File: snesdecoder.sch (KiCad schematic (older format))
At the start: 17 parts, among them J1 SNES Controller Input, J2 UpDownLeftRight, J3 AB, J4 XY, J5 StartSel, J6 LR, J7 Power, U1 74HC04, U2 74LS161, U3 TPIC6C596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

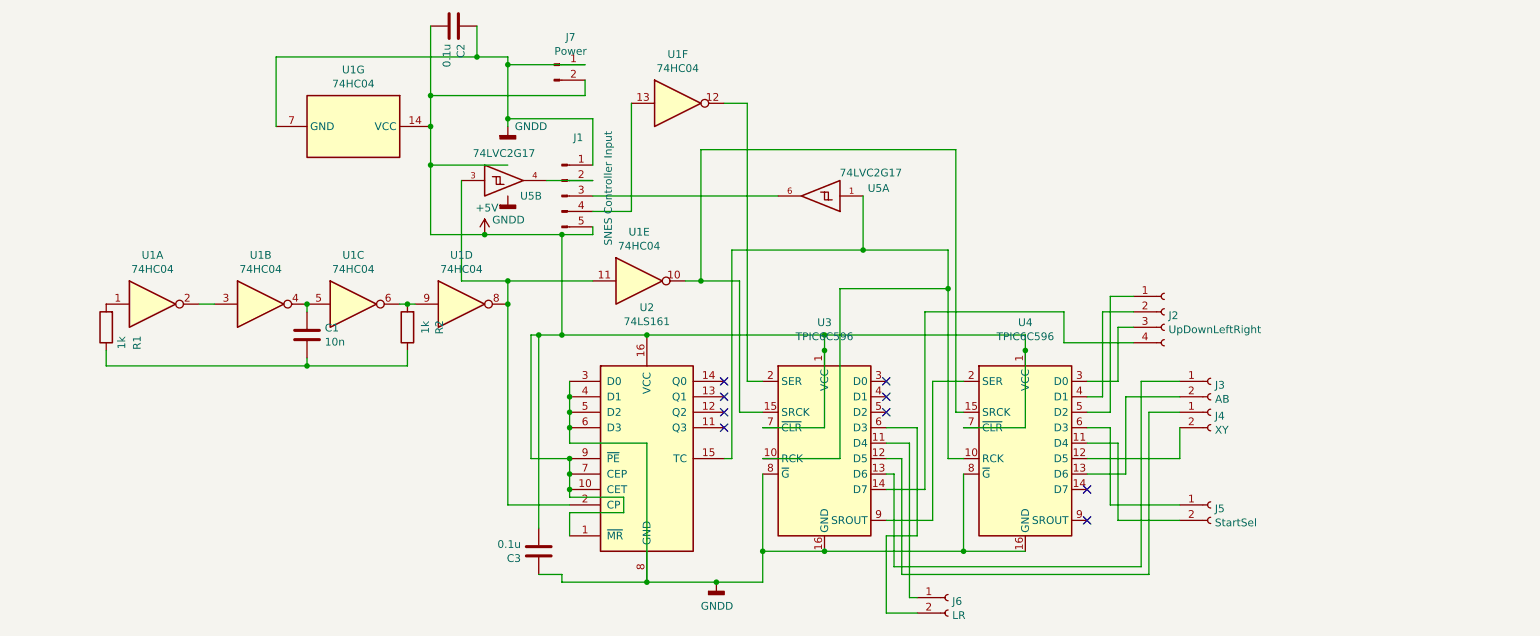
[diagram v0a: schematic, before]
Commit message: update to V2: change schema, pcb layout, datasheets
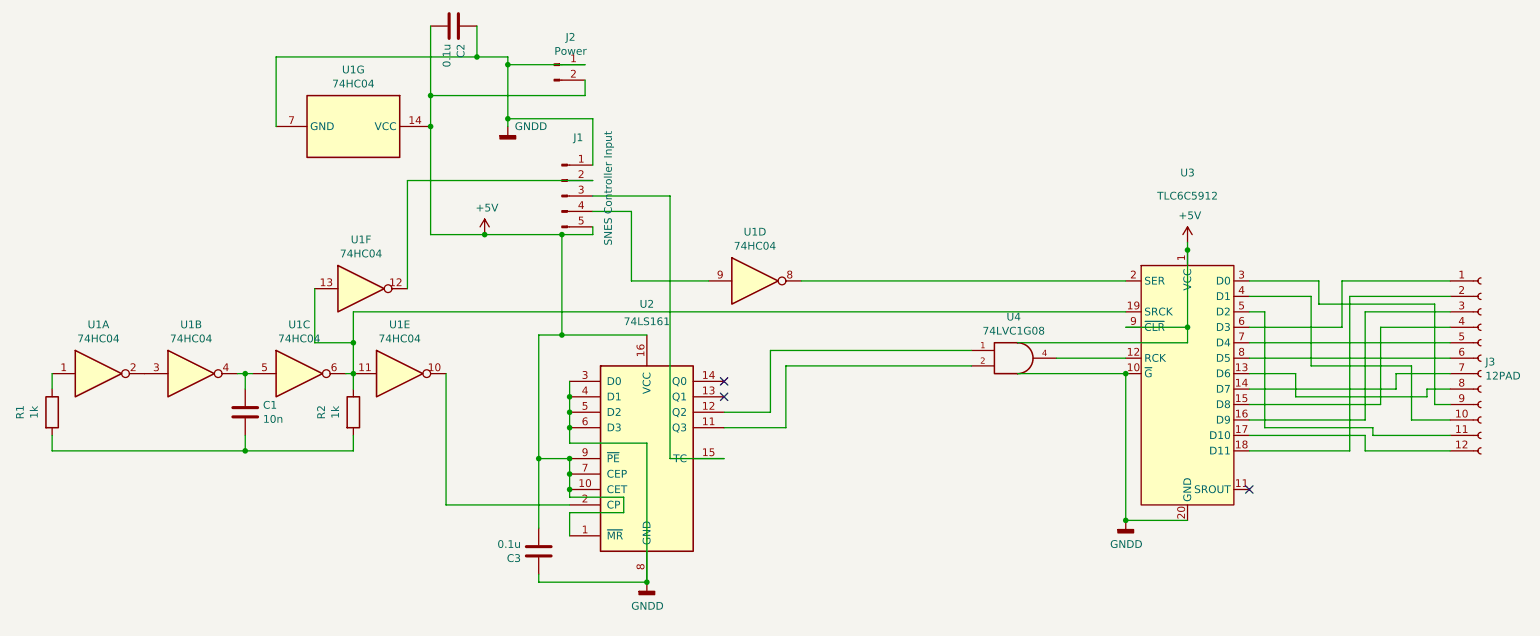
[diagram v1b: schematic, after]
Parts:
- removed J2: UpDownLeftRight, IO:4PAD_DIR, symbol Connector:Conn_01x04_Female
- removed J3: AB, IO:2PAD_AB, symbol Connector:Conn_01x02_Female
- removed J4: XY, IO:2PAD_XY, symbol Connector:Conn_01x02_Female
- removed J5: StartSel, IO:2PAD_StartSel, symbol Connector:Conn_01x02_Female
- removed J6: LR, IO:2PAD_LR, symbol Connector:Conn_01x02_Female
- removed U3, U4: TPIC6C596, Package_SO:SOIC-16_3.9x9.9mm_P1.27mm, symbol newchips:TPIC6C596
- removed U5: 74LVC2G17, Package_SO:SC-74-6_1.5x2.9mm_P0.95mm, symbol 74xGxx:74LVC2G17
- added J3: 12PAD, IO:12PAD, symbol Connector:Conn_01x12_Female
- added U3: TLC6C5912, Package_SO:SOIC-20W_7.5x12.8mm_P1.27mm, symbol newchips:TLC6C5912
- added U4: 74LVC1G08, Package_TO_SOT_SMD:SOT-353_SC-70-5_Handsoldering, symbol 74xGxx:74LVC1G08
- renumbered J7 to J2
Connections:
- net +5V: now also U3.1 (VCC), U3.9 (~CLR), U4.5 (VCC)
- net GND: now also U3.10 (~G), U3.20 (GND), U4.3 (GND)
- net at R1.2: now also C1.2, R2.2; no longer U1.1
- net at U2.11 (Q3): now also U4.2
- net at U2.12 (Q2): now also U4.1
- net at U2.15 (TC): now also J1.3 (Pin_3)
- net at J1.2 (Pin_2): now also U1.12
- net at J1.4 (Pin_4): now also U1.9; no longer U1.13
- net at U1.10: now also U2.2 (CP)
- new net: R2.1, U1.11, U1.13, U1.6, U3.19 (SRCK)
- new net: J3.1 (Pin_1), U3.6 (D3)
- new net: J3.10 (Pin_10), U3.4 (D1)
- new net: J3.11 (Pin_11), U3.5 (D2)
- new net: J3.12 (Pin_12), U3.17 (D10)
- new net: J3.2 (Pin_2), U3.18 (D11)
- new net: J3.3 (Pin_3), U3.16 (D9)
- new net: J3.4 (Pin_4), U3.15 (D8)
- new net: J3.5 (Pin_5), U3.7 (D4)
- new net: J3.6 (Pin_6), U3.8 (D5)
- new net: J3.7 (Pin_7), U3.14 (D7)
- new net: J3.8 (Pin_8), U3.13 (D6)
- new net: J3.9 (Pin_9), U3.3 (D0)
- new net: R1.1, U1.1
- new net: U3.12 (RCK), U4.4
- new net: U1.8, U3.2 (SER)
- no-connect marks 9 -> 3
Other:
- moved on the sheet: C1, R2

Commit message: gerbers to v2
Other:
- moved on the sheet: J3, U3, U4
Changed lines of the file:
@@
 L newchips:TLC6C5912 U3
 U 1 1 5FB36650
-P 8200 3350
-F 0 "U3" H 8200 4450 50  0000 C CNN
-F 1 "TLC6C5912" H 8200 4300 50  0000 C CNN
-F 2 "Package_SO:SOIC-20W_7.5x12.8mm_P1.27mm" H 8600 2650 50  0001 C CNN
-F 3 "" H 8600 2650 50  0001 C CNN
-	1    8200 3350
-	1    0    0    -1
-$EndComp
-Wire Wire Line
-	5700 2950 7800 2950
-Wire Wire Line
-	7350 3450 7800 3450
-Wire Wire Line
-	7800 3550 7800 4500
-Wire Wire Line
-	7800 4500 8200 4500
+P 7000 3350
+F 0 "U3" H 7000 4450 50  0000 C CNN
+F 1 "TLC6C5912" H 7000 4300 50  0000 C CNN
+F 2 "Package_SO:SOIC-20W_7.5x12.8mm_P1.27mm" H 7400 2650 50  0001 C CNN
+F 3 "" H 7400 2650 50  0001 C CNN
+	1    7000 3350
+	1    0    0    -1
+$EndComp
+Wire Wire Line
+	6150 3450 6600 3450
+Wire Wire Line
+	6600 3550 6600 4500
+Wire Wire Line
+	6600 4500 7000 4500
 $Comp
 L power:GNDD #PWR0101
 U 1 1 5FB3EC8C
-P 7800 4500
-F 0 "#PWR0101" H 7800 4250 50  0001 C CNN
-F 1 "GNDD" H 7804 4345 50  0000 C CNN
-F 2 "" H 7800 4500 50  0001 C CNN
-F 3 "" H 7800 4500 50  0001 C CNN
-	1    7800 4500
-	1    0    0    -1
-$EndComp
-Connection ~ 7800 4500
+P 6600 4500
+F 0 "#PWR0101" H 6600 4250 50  0001 C CNN
+F 1 "GNDD" H 6604 4345 50  0000 C CNN
+F 2 "" H 6600 4500 50  0001 C CNN
+F 3 "" H 6600 4500 50  0001 C CNN
+	1    6600 4500
+	1    0    0    -1
+$EndComp
+Connection ~ 6600 4500
 $Comp
 L power:+5V #PWR0102
 U 1 1 5FB41555
-P 8200 2700
-F 0 "#PWR0102" H 8200 2550 50  0001 C CNN
-F 1 "+5V" H 8215 2873 50  0000 C CNN
-F 2 "" H 8200 2700 50  0001 C CNN
-F 3 "" H 8200 2700 50  0001 C CNN
-	1    8200 2700
+P 7000 2700
+F 0 "#PWR0102" H 7000 2550 50  0001 C CNN
+F 1 "+5V" H 7015 2873 50  0000 C CNN
+F 2 "" H 7000 2700 50  0001 C CNN
+F 3 "" H 7000 2700 50  0001 C CNN
+	1    7000 2700
 	1    0    0    -1
 $EndComp
@@
 	4850 2400 4350 2400
 Wire Wire Line
-	7800 3250 8200 3250
-Wire Wire Line
-	8200 3250 8200 2750
-Wire Wire Line
-	8200 2750 8200 2700
-Connection ~ 8200 2750
+	6600 3250 7000 3250
+Wire Wire Line
+	7000 3250 7000 2750
+Wire Wire Line
+	7000 2750 7000 2700
+Connection ~ 7000 2750
 NoConn ~ 5200 3600
 NoConn ~ 5200 3700
-NoConn ~ 8600 4300
+NoConn ~ 7400 4300
 $Comp
 L 74xGxx:74LVC1G08 U4
 U 1 1 5FB0C867
-P 7100 3450
-F 0 "U4" H 7075 3717 50  0000 C CNN
-F 1 "74LVC1G08" H 7075 3626 50  0000 C CNN
-F 2 "Package_TO_SOT_SMD:SOT-353_SC-70-5_Handsoldering" H 7100 3450 50  0001 C CNN
-F 3 "http://www.ti.com/lit/sg/scyt129e/scyt129e.pdf" H 7100 3450 50  0001 C CNN
-	1    7100 3450
+P 5900 3450
+F 0 "U4" H 5875 3717 50  0000 C CNN
+F 1 "74LVC1G08" H 5875 3626 50  0000 C CNN
+F 2 "Package_TO_SOT_SMD:SOT-353_SC-70-5_Handsoldering" H 5900 3450 50  0001 C CNN
+F 3 "http://www.ti.com/lit/sg/scyt129e/scyt129e.pdf" H 5900 3450 50  0001 C CNN
+	1    5900 3450
 	1    0    0    -1
 $EndComp
@@
 	5500 3800 5500 3400
 Wire Wire Line
-	5500 3400 6800 3400
-Wire Wire Line
 	5600 3900 5600 3500
 Wire Wire Line
-	5600 3500 6800 3500
-Wire Wire Line
 	5200 3900 5600 3900
 Wire Wire Line
-	7100 3350 8200 3350
-Wire Wire Line
-	8200 3350 8200 3250
-Connection ~ 8200 3250
-Wire Wire Line
-	7100 3550 7800 3550
-Connection ~ 7800 3550
+	5900 3350 7000 3350
+Wire Wire Line
+	7000 3350 7000 3250
+Connection ~ 7000 3250
+Wire Wire Line
+	5900 3550 6600 3550
+Connection ~ 6600 3550
 $Comp
 L Device:R R2
@@
 Wire Wire Line
 	2800 3150 2800 3350
-Wire Wire Line
-	2800 3150 7800 3150
 Connection ~ 2800 3350
 $Comp
 L Connector:Conn_01x12_Female J3
 U 1 1 5FAF303D
-P 10100 3450
-F 0 "J3" H 10128 3426 50  0000 L CNN
-F 1 "12PAD" H 10128 3335 50  0000 L CNN
-F 2 "IO:12PAD" H 10100 3450 50  0001 C CNN
-F 3 "~" H 10100 3450 50  0001 C CNN
-	1    10100 3450
-	1    0    0    -1
-$EndComp
-Wire Wire Line
-	8600 4050 9250 4050
-Wire Wire Line
-	9250 4050 9250 3050
-Wire Wire Line
-	9250 3050 9900 3050
-Wire Wire Line
-	8600 3950 9350 3950
-Wire Wire Line
-	9350 3950 9350 4050
-Wire Wire Line
-	9350 4050 9900 4050
-Wire Wire Line
-	8600 3850 9350 3850
-Wire Wire Line
-	9350 3850 9350 3150
-Wire Wire Line
-	9350 3150 9900 3150
-Wire Wire Line
-	8600 3750 9450 3750
-Wire Wire Line
-	9450 3750 9450 3250
-Wire Wire Line
-	9450 3250 9900 3250
-Wire Wire Line
-	9550 3650 9550 3550
-Wire Wire Line
-	9550 3550 9900 3550
-Wire Wire Line
-	8600 3650 9550 3650
-Wire Wire Line
-	8600 3550 8900 3550
-Wire Wire Line
-	8900 3550 8900 3700
-Wire Wire Line
-	8900 3700 9750 3700
-Wire Wire Line
-	9750 3700 9750 3650
-Wire Wire Line
-	9750 3650 9900 3650
-Wire Wire Line
-	8600 3450 9900 3450
-Wire Wire Line
-	9900 3350 8600 3350
-Wire Wire Line
-	8600 3250 9200 3250
-Wire Wire Line
-	9200 3250 9200 2950
-Wire Wire Line
-	9200 2950 9900 2950
-Wire Wire Line
-	8600 3150 8700 3150
-Wire Wire Line
-	8700 3150 8700 3900
-Wire Wire Line
-	8700 3900 9400 3900
-Wire Wire Line
-	9400 3900 9400 3950
-Wire Wire Line
-	9400 3950 9900 3950
-Wire Wire Line
-	8600 3050 9000 3050
-Wire Wire Line
-	9000 3050 9000 3500
-Wire Wire Line
-	9000 3500 9650 3500
-Wire Wire Line
-	9650 3500 9650 3850
-Wire Wire Line
-	9650 3850 9900 3850
-Wire Wire Line
-	9900 3750 9800 3750
-Wire Wire Line
-	9800 3750 9800 3100
-Wire Wire Line
-	9800 3100 9050 3100
-Wire Wire Line
-	9050 3100 9050 2950
-Wire Wire Line
-	9050 2950 8600 2950
+P 8900 3450
+F 0 "J3" H 8928 3426 50  0000 L CNN
+F 1 "12PAD" H 8928 3335 50  0000 L CNN
+F 2 "IO:12PAD" H 8900 3450 50  0001 C CNN
+F 3 "~" H 8900 3450 50  0001 C CNN
+	1    8900 3450
+	1    0    0    -1
+$EndComp
+Wire Wire Line
+	7400 4050 8050 4050
+Wire Wire Line
+	8050 4050 8050 3050
+Wire Wire Line
+	8050 3050 8700 3050
+Wire Wire Line
+	7400 3950 8150 3950
+Wire Wire Line
+	8150 3950 8150 4050
+Wire Wire Line
+	8150 4050 8700 4050
+Wire Wire Line
+	7400 3850 8150 3850
+Wire Wire Line
+	8150 3850 8150 3150
+Wire Wire Line
+	8150 3150 8700 3150
+Wire Wire Line
+	7400 3750 8250 3750
+Wire Wire Line
+	8250 3750 8250 3250
+Wire Wire Line
+	8250 3250 8700 3250
+Wire Wire Line
+	8350 3650 8350 3550
+Wire Wire Line
+	8350 3550 8700 3550
+Wire Wire Line
+	7400 3650 8350 3650
+Wire Wire Line
+	7400 3550 7700 3550
+Wire Wire Line
+	7700 3550 7700 3700
+Wire Wire Line
+	7700 3700 8550 3700
+Wire Wire Line
+	8550 3700 8550 3650
+Wire Wire Line
+	8550 3650 8700 3650
+Wire Wire Line
+	7400 3450 8700 3450
+Wire Wire Line
+	8700 3350 7400 3350
+Wire Wire Line
+	7400 3250 8000 3250
+Wire Wire Line
+	8000 3250 8000 2950
+Wire Wire Line
+	8000 2950 8700 2950
+Wire Wire Line
+	7400 3150 7500 3150
+Wire Wire Line
+	7500 3150 7500 3900
+Wire Wire Line
+	7500 3900 8200 3900
+Wire Wire Line
+	8200 3900 8200 3950
+Wire Wire Line
+	8200 3950 8700 3950
+Wire Wire Line
+	7400 3050 7800 3050
+Wire Wire Line
+	7800 3050 7800 3500
+Wire Wire Line
+	7800 3500 8450 3500
+Wire Wire Line
+	8450 3500 8450 3850
+Wire Wire Line
+	8450 3850 8700 3850
+Wire Wire Line
+	8700 3750 8600 3750
+Wire Wire Line
+	8600 3750 8600 3100
+Wire Wire Line
+	8600 3100 7850 3100
+Wire Wire Line
+	7850 3100 7850 2950
+Wire Wire Line
+	7850 2950 7400 2950
+Wire Wire Line
+	5700 2950 6600 2950
+Wire Wire Line
+	6600 3150 2800 3150
+Wire Wire Line
+	5500 3400 5600 3400
 $EndSCHEMATC

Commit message: fix sch
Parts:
- U1: footprint Package_SO:SOIC-14_3.9x8.7mm_P1.27mm -> Package_SO:TSSOP-14_4.4x5mm_P0.65mm
- U2: footprint Package_SO:SOIC-16_3.9x9.9mm_P1.27mm -> Package_SO:TSSOP-16_4.4x5mm_P0.65mm
- U3: footprint Package_SO:SOIC-20W_7.5x12.8mm_P1.27mm -> Package_SO:TSSOP-20_4.4x6.5mm_P0.65mm
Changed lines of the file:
@@
 F 0 "U2" H 4700 5100 50  0000 C CNN
 F 1 "74LS161" H 4700 4987 50  0000 C CNN
-F 2 "Package_SO:SOIC-16_3.9x9.9mm_P1.27mm" H 4700 4100 50  0001 C CNN
+F 2 "Package_SO:TSSOP-16_4.4x5mm_P0.65mm" H 4700 4100 50  0001 C CNN
 F 3 "http://www.ti.com/lit/gpn/sn74LS161" H 4700 4100 50  0001 C CNN
 	1    4700 4100
@@
 F 0 "U3" H 7000 4450 50  0000 C CNN
 F 1 "TLC6C5912" H 7000 4300 50  0000 C CNN
-F 2 "Package_SO:SOIC-20W_7.5x12.8mm_P1.27mm" H 7400 2650 50  0001 C CNN
+F 2 "Package_SO:TSSOP-20_4.4x6.5mm_P0.65mm" H 7400 2650 50  0001 C CNN
 F 3 "" H 7400 2650 50  0001 C CNN
 	1    7000 3350
@@
 F 0 "U1" H 1150 3867 50  0000 C CNN
 F 1 "74HC04" H 1150 3776 50  0000 C CNN
-F 2 "Package_SO:SOIC-14_3.9x8.7mm_P1.27mm" H 1150 3550 50  0001 C CNN
+F 2 "Package_SO:TSSOP-14_4.4x5mm_P0.65mm" H 1150 3550 50  0001 C CNN
 F 3 "https://assets.nexperia.com/documents/data-sheet/74HC_HCT04.pdf" H 1150 3550 50  0001 C CNN
 	1    1150 3550
@@
 F 0 "U1" H 1750 3867 50  0000 C CNN
 F 1 "74HC04" H 1750 3776 50  0000 C CNN
-F 2 "Package_SO:SOIC-14_3.9x8.7mm_P1.27mm" H 1750 3550 50  0001 C CNN
+F 2 "Package_SO:TSSOP-14_4.4x5mm_P0.65mm" H 1750 3550 50  0001 C CNN
 F 3 "https://assets.nexperia.com/documents/data-sheet/74HC_HCT04.pdf" H 1750 3550 50  0001 C CNN
 	2    1750 3550
@@
 F 0 "U1" H 2450 3867 50  0000 C CNN
 F 1 "74HC04" H 2450 3776 50  0000 C CNN
-F 2 "Package_SO:SOIC-14_3.9x8.7mm_P1.27mm" H 2450 3550 50  0001 C CNN
+F 2 "Package_SO:TSSOP-14_4.4x5mm_P0.65mm" H 2450 3550 50  0001 C CNN
 F 3 "https://assets.nexperia.com/documents/data-sheet/74HC_HCT04.pdf" H 2450 3550 50  0001 C CNN
 	3    2450 3550
@@
 F 0 "U1" V 2433 1950 50  0000 C CNN
 F 1 "74HC04" V 2524 1950 50  0000 C CNN
-F 2 "Package_SO:SOIC-14_3.9x8.7mm_P1.27mm" H 2800 1950 50  0001 C CNN
+F 2 "Package_SO:TSSOP-14_4.4x5mm_P0.65mm" H 2800 1950 50  0001 C CNN
 F 3 "https://assets.nexperia.com/documents/data-sheet/74HC_HCT04.pdf" H 2800 1950 50  0001 C CNN
 	7    2800 1950
@@
 F 0 "U1" H 5400 3267 50  0000 C CNN
 F 1 "74HC04" H 5400 3176 50  0000 C CNN
-F 2 "Package_SO:SOIC-14_3.9x8.7mm_P1.27mm" H 5400 2950 50  0001 C CNN
+F 2 "Package_SO:TSSOP-14_4.4x5mm_P0.65mm" H 5400 2950 50  0001 C CNN
 F 3 "https://assets.nexperia.com/documents/data-sheet/74HC_HCT04.pdf" H 5400 2950 50  0001 C CNN
 	4    5400 2950
@@
 F 0 "U1" H 3100 3867 50  0000 C CNN
 F 1 "74HC04" H 3100 3776 50  0000 C CNN
-F 2 "Package_SO:SOIC-14_3.9x8.7mm_P1.27mm" H 3100 3550 50  0001 C CNN
+F 2 "Package_SO:TSSOP-14_4.4x5mm_P0.65mm" H 3100 3550 50  0001 C CNN
 F 3 "https://assets.nexperia.com/documents/data-sheet/74HC_HCT04.pdf" H 3100 3550 50  0001 C CNN
 	5    3100 3550
@@
 F 0 "U1" H 2850 3317 50  0000 C CNN
 F 1 "74HC04" H 2850 3226 50  0000 C CNN
-F 2 "Package_SO:SOIC-14_3.9x8.7mm_P1.27mm" H 2850 3000 50  0001 C CNN
+F 2 "Package_SO:TSSOP-14_4.4x5mm_P0.65mm" H 2850 3000 50  0001 C CNN
 F 3 "https://assets.nexperia.com/documents/data-sheet/74HC_HCT04.pdf" H 2850 3000 50  0001 C CNN
 	6    2850 3000
